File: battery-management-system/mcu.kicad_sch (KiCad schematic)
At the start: 34 parts, among them J11 I2C, J12 MCU_SUPPLY, J13 LEDS, J19 CHARGE/DISCHARGE, J20 UART_INTERCONNECT, J21 UART_USB, U14 STC3100, U4 STM32L071CZTx, U5 ARM-JTAG-SWD, U8 AT24C512C, U9 NCT75DR2G

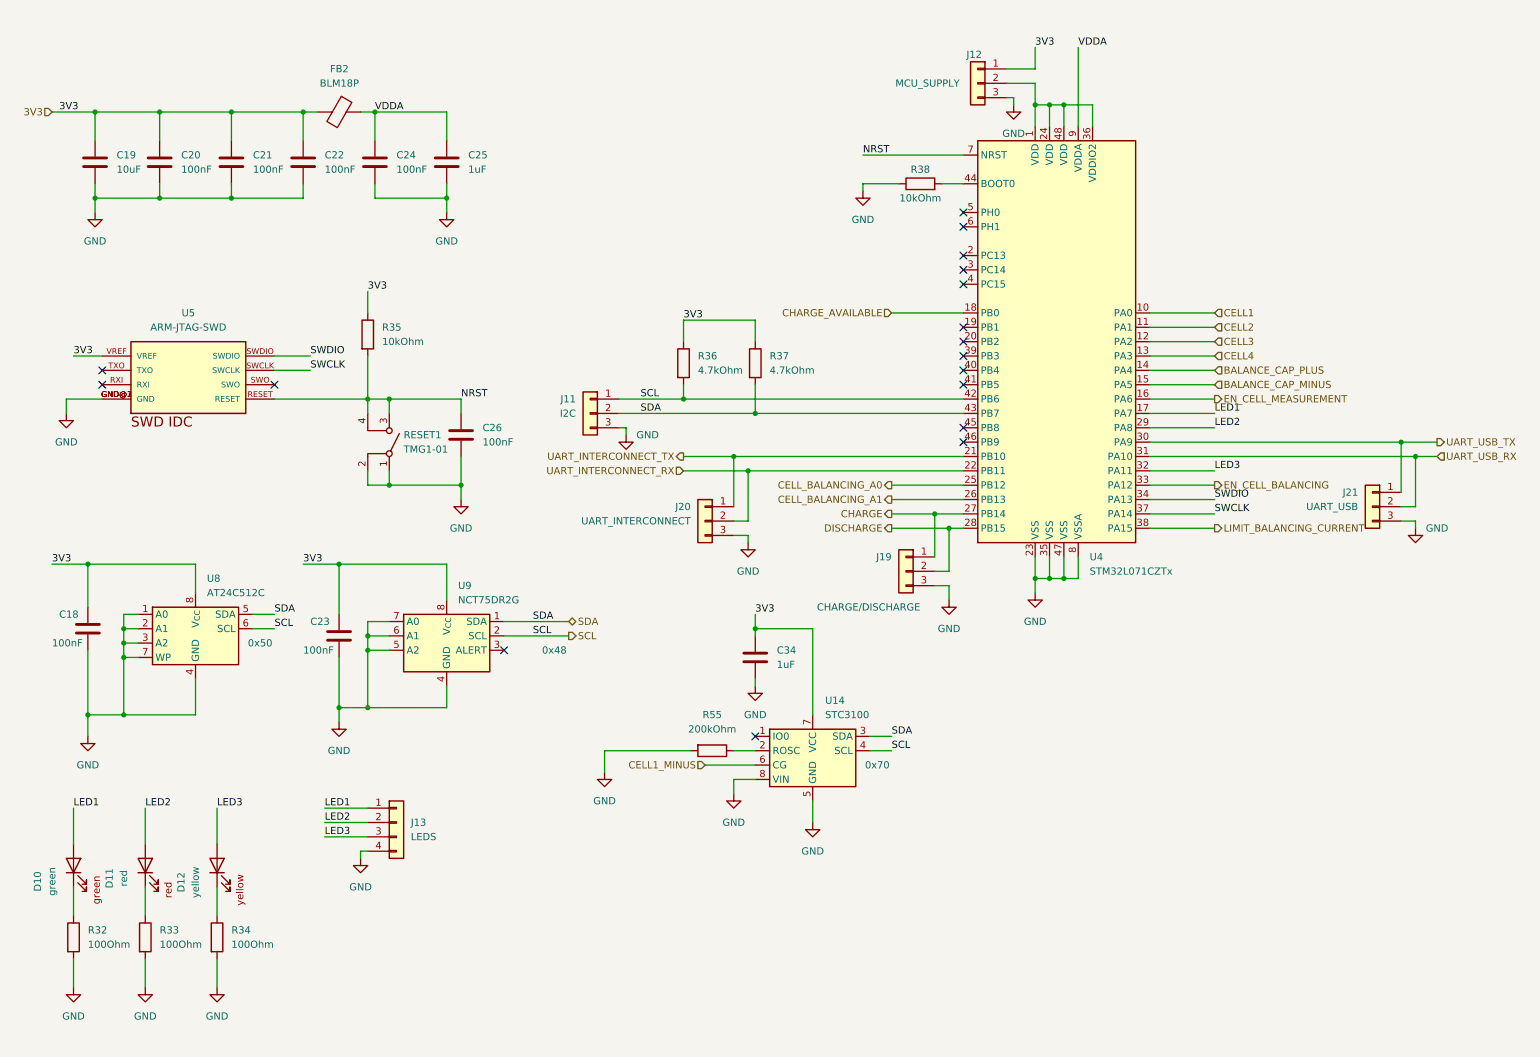
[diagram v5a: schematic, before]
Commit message: fix current sensing
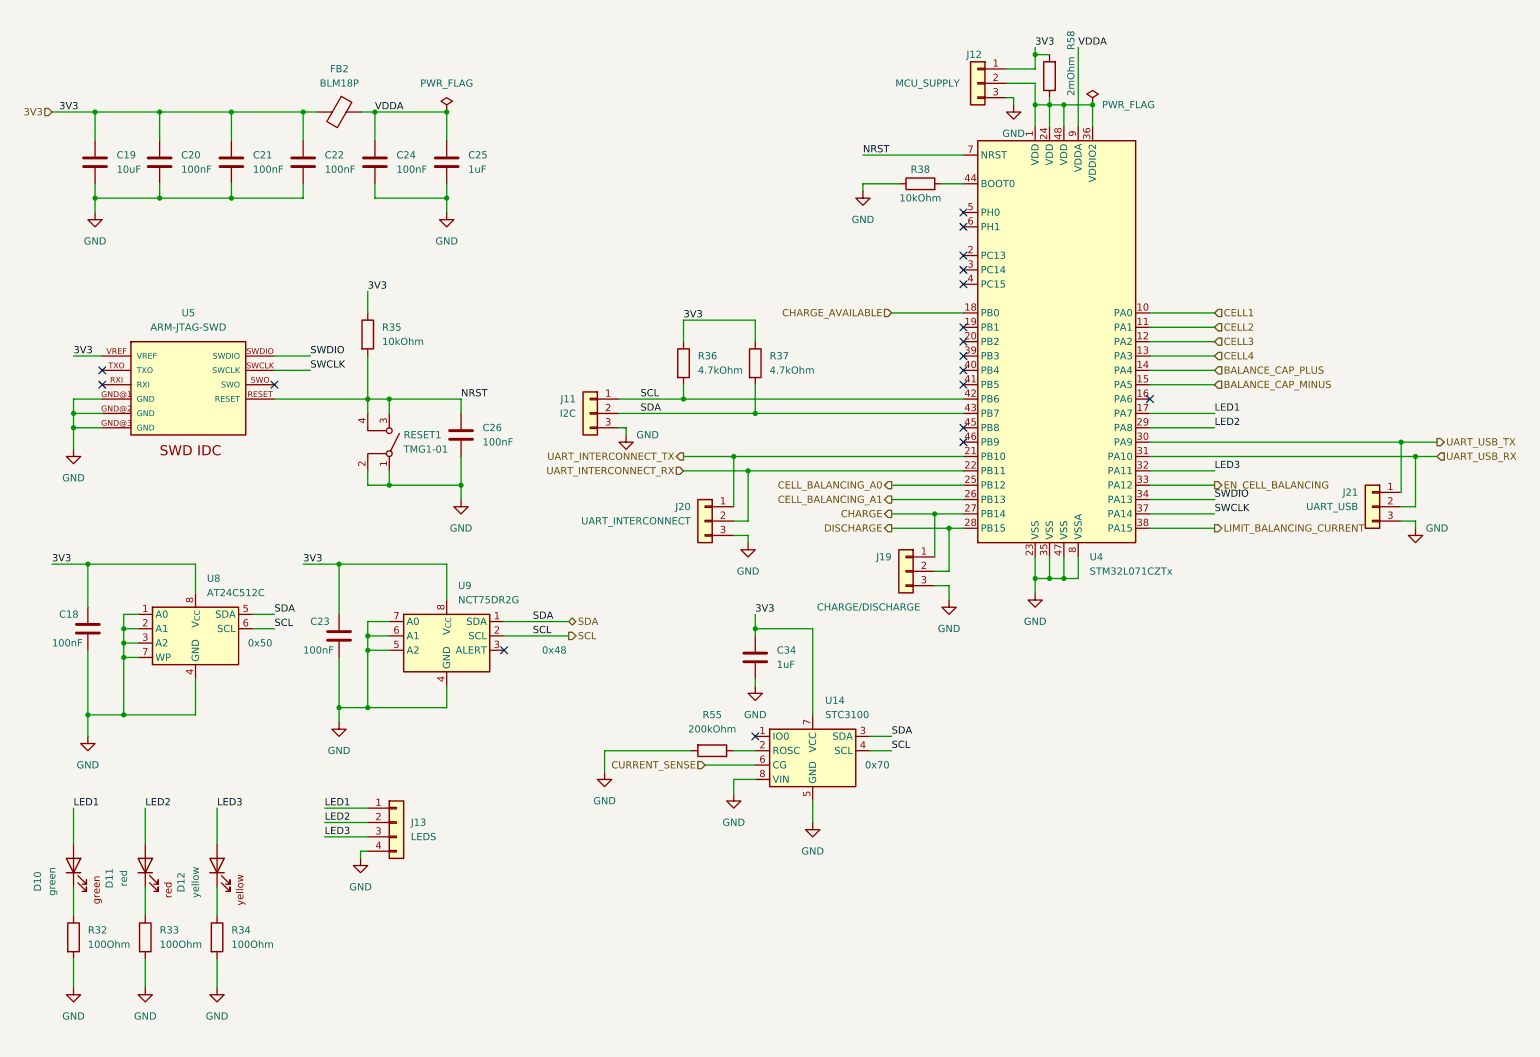
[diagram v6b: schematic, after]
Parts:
- added R58: 2mOhm, benediktibk:R_2512_6332Metric_Pad1.40x3.35mm_HandSolder, symbol benediktibk:R_2mOhm_SMD_2512_5W_1%
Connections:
- net 3V3: now also R58.2
- net at J12.2 (Pin_2), U4.1 (VDD), U4.24 (VDD)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: now also R58.1
- net CELL1_MINUS renamed CURRENT_SENSE
- net EN_CELL_MEASUREMENT: no longer names the net of U4.16 (PA6)
- no-connect marks 17 -> 18
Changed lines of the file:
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@@
   (junction (at 36.83 124.46) (diameter 0) (color 0 0 0 0)
   )
+  (junction (at 27.94 86.36) (diameter 0) (color 0 0 0 0)
+  )
   (junction (at 43.18 30.48) (diameter 0) (color 0 0 0 0)
   )
+  (junction (at 27.94 83.82) (diameter 0) (color 0 0 0 0)
+  )
   (junction (at 203.2 113.03) (diameter 0) (color 0 0 0 0)
   )
+  (junction (at 93.98 30.48) (diameter 0) (color 0 0 0 0)
+  )
   (junction (at 80.01 125.73) (diameter 0) (color 0 0 0 0)
   )
@@
   (junction (at 43.18 45.72) (diameter 0) (color 0 0 0 0)
   )
+  (junction (at 208.28 29.21) (diameter 0) (color 0 0 0 0)
+  )
   (junction (at 74.93 110.49) (diameter 0) (color 0 0 0 0)
   )
@@
   )
   (junction (at 198.12 29.21) (diameter 0) (color 0 0 0 0)
+  )
+  (junction (at 198.12 20.32) (diameter 0) (color 0 0 0 0)
   )
   (junction (at 68.58 30.48) (diameter 0) (color 0 0 0 0)
@@
   (no_connect (at 185.42 60.96))
   (no_connect (at 185.42 71.12))
+  (no_connect (at 218.44 81.28))
   (no_connect (at 185.42 55.88))
   (no_connect (at 185.42 78.74))
@@
     (stroke (width 0) (type default))
   )
+  (wire (pts (xy 200.66 27.94) (xy 200.66 29.21))
+    (stroke (width 0) (type default))
+  )
   (wire (pts (xy 125.73 86.36) (xy 124.46 86.36))
     (stroke (width 0) (type default))
@@
     (stroke (width 0) (type default))
   )
+  (wire (pts (xy 27.94 86.36) (xy 33.02 86.36))
+    (stroke (width 0) (type default))
+  )
   (wire (pts (xy 135.89 93.98) (xy 147.32 93.98))
     (stroke (width 0) (type default))
@@
     (stroke (width 0) (type default))
   )
-  (wire (pts (xy 218.44 81.28) (xy 229.87 81.28))
-    (stroke (width 0) (type default))
-  )
   (wire (pts (xy 55.88 45.72) (xy 68.58 45.72))
     (stroke (width 0) (type default))
@@
     (stroke (width 0) (type default))
   )
-  (wire (pts (xy 33.02 81.28) (xy 26.67 81.28))
+  (wire (pts (xy 33.02 81.28) (xy 27.94 81.28))
     (stroke (width 0) (type default))
   )
@@
     (stroke (width 0) (type default))
   )
-  (wire (pts (xy 26.67 81.28) (xy 26.67 83.82))
+  (wire (pts (xy 27.94 81.28) (xy 27.94 83.82))
     (stroke (width 0) (type default))
   )
@@
     (stroke (width 0) (type default))
   )
+  (wire (pts (xy 198.12 20.32) (xy 200.66 20.32))
+    (stroke (width 0) (type default))
+  )
   (wire (pts (xy 182.88 114.3) (xy 180.34 114.3))
     (stroke (width 0) (type default))
@@
     (stroke (width 0) (type default))
   )
+  (wire (pts (xy 27.94 83.82) (xy 33.02 83.82))
+    (stroke (width 0) (type default))
+  )
   (wire (pts (xy 36.83 137.16) (xy 49.53 137.16))
     (stroke (width 0) (type default))
@@
     (stroke (width 0) (type default))
   )
-  (wire (pts (xy 198.12 19.05) (xy 198.12 22.86))
+  (wire (pts (xy 198.12 19.05) (xy 198.12 20.32))
     (stroke (width 0) (type default))
   )
@@
     (stroke (width 0) (type default))
   )
+  (wire (pts (xy 27.94 83.82) (xy 27.94 86.36))
+    (stroke (width 0) (type default))
+  )
   (wire (pts (xy 36.83 127) (xy 36.83 124.46))
     (stroke (width 0) (type default))
@@
     (stroke (width 0) (type default))
   )
+  (wire (pts (xy 198.12 20.32) (xy 198.12 22.86))
+    (stroke (width 0) (type default))
+  )
   (wire (pts (xy 80.01 93.98) (xy 80.01 96.52))
     (stroke (width 0) (type default))
@@
   )
   (wire (pts (xy 30.48 137.16) (xy 36.83 137.16))
+    (stroke (width 0) (type default))
+  )
+  (wire (pts (xy 27.94 86.36) (xy 27.94 90.17))
     (stroke (width 0) (type default))
   )
@@
     (effects (font (size 1.27 1.27)) (justify left))
   )
-  (hierarchical_label "EN_CELL_MEASUREMENT" (shape output) (at 229.87 81.28 0) (fields_autoplaced)
-    (effects (font (size 1.27 1.27)) (justify left))
-  )
   (hierarchical_label "3V3" (shape input) (at 24.13 30.48 180) (fields_autoplaced)
     (effects (font (size 1.27 1.27)) (justify right))
@@
     (effects (font (size 1.27 1.27)) (justify left))
   )
-  (hierarchical_label "CELL1_MINUS" (shape input) (at 139.7 146.05 180) (fields_autoplaced)
+  (hierarchical_label "CURRENT_SENSE" (shape input) (at 139.7 146.05 180) (fields_autoplaced)
     (effects (font (size 1.27 1.27)) (justify right))
   )
@@
         (path "/5272f0ff-3069-41a9-bca2-80beede8b4b2/409f87d1-afa6-40d2-ba42-d5009501b8f9"
           (reference "C20") (unit 1)
+        )
+      )
+    )
+  )
+  (symbol (lib_id "power:PWR_FLAG") (at 93.98 30.48 0) (unit 1)
+    (in_bom yes) (on_board yes) (dnp no) (fields_autoplaced)
+    (property "Reference" "#FLG05" (at 93.98 28.575 0)
+      (effects (font (size 1.27 1.27)) hide)
+    )
+    (property "Value" "PWR_FLAG" (at 93.98 25.4 0)
+      (effects (font (size 1.27 1.27)))
+    )
+    (property "Footprint" "" (at 93.98 30.48 0)
+      (effects (font (size 1.27 1.27)) hide)
+    )
+    (property "Datasheet" "~" (at 93.98 30.48 0)
+      (effects (font (size 1.27 1.27)) hide)
+    )
+    (pin "1")
+    (instances
+      (project "battery-management-system"
+        (path "/5272f0ff-3069-41a9-bca2-80beede8b4b2/afdb149d-bd78-484c-a496-c5b66260efca"
+          (reference "#FLG05") (unit 1)
+        )
+        (path "/5272f0ff-3069-41a9-bca2-80beede8b4b2/409f87d1-afa6-40d2-ba42-d5009501b8f9"
+          (reference "#FLG06") (unit 1)
         )
       )
@@
     )
   )
+  (symbol (lib_id "power:PWR_FLAG") (at 208.28 29.21 0) (unit 1)
+    (in_bom yes) (on_board yes) (dnp no)
+    (property "Reference" "#FLG05" (at 208.28 27.305 0)
+      (effects (font (size 1.27 1.27)) hide)
+    )
+    (property "Value" "PWR_FLAG" (at 214.63 29.21 0)
+      (effects (font (size 1.27 1.27)))
+    )
+    (property "Footprint" "" (at 208.28 29.21 0)
+      (effects (font (size 1.27 1.27)) hide)
+    )
+    (property "Datasheet" "~" (at 208.28 29.21 0)
+      (effects (font (size 1.27 1.27)) hide)
+    )
+    (pin "1")
+    (instances
+      (project "battery-management-system"
+        (path "/5272f0ff-3069-41a9-bca2-80beede8b4b2/afdb149d-bd78-484c-a496-c5b66260efca"
+          (reference "#FLG05") (unit 1)
+        )
+        (path "/5272f0ff-3069-41a9-bca2-80beede8b4b2/409f87d1-afa6-40d2-ba42-d5009501b8f9"
+          (reference "#FLG07") (unit 1)
+        )
+      )
+    )
+  )
   (symbol (lib_id "power:GND") (at 93.98 48.26 0) (unit 1)
     (in_bom yes) (on_board yes) (dnp no) (fields_autoplaced)
@@
     )
   )
-  (symbol (lib_id "power:GND") (at 26.67 83.82 0) (unit 1)
-    (in_bom yes) (on_board yes) (dnp no) (fields_autoplaced)
-    (property "Reference" "#PWR0138" (at 26.67 90.17 0)
-      (effects (font (size 1.27 1.27)) hide)
-    )
-    (property "Value" "GND" (at 26.67 88.9 0)
-      (effects (font (size 1.27 1.27)))
-    )
-    (property "Footprint" "" (at 26.67 83.82 0)
-      (effects (font (size 1.27 1.27)) hide)
-    )
-    (property "Datasheet" "" (at 26.67 83.82 0)
+  (symbol (lib_id "power:GND") (at 27.94 90.17 0) (unit 1)
+    (in_bom yes) (on_board yes) (dnp no) (fields_autoplaced)
+    (property "Reference" "#PWR0138" (at 27.94 96.52 0)
+      (effects (font (size 1.27 1.27)) hide)
+    )
+    (property "Value" "GND" (at 27.94 95.25 0)
+      (effects (font (size 1.27 1.27)))
+    )
+    (property "Footprint" "" (at 27.94 90.17 0)
+      (effects (font (size 1.27 1.27)) hide)
+    )
+    (property "Datasheet" "" (at 27.94 90.17 0)
       (effects (font (size 1.27 1.27)) hide)
     )
@@
         )
       )
+    )
+  )
+  (symbol (lib_id "benediktibk:R_2mOhm_SMD_2512_5W_1%") (at 200.66 24.13 180) (unit 1)
+    (in_bom yes) (on_board yes) (dnp no)
+    (property "Reference" "R58" (at 204.47 17.78 90)
+      (effects (font (size 1.27 1.27)))
+    )
+    (property "Value" "2mOhm" (at 204.47 24.13 90)
+      (effects (font (size 1.27 1.27)))
+    )
+    (property "Footprint" "benediktibk:R_2512_6332Metric_Pad1.40x3.35mm_HandSolder" (at 210.82 24.638 90)
+      (effects (font (size 1.27 1.27)) hide)
+    )
+    (property "Datasheet" "~" (at 200.66 24.13 0)
+      (effects (font (size 1.27 1.27)) hide)
+    )
+    (property "RS order number" "231-3683" (at 218.44 25.4 0)
+      (effects (font (size 1.27 1.27)) hide)
+    )
+    (pin "1")
+    (pin "2")
+    (instances
+      (project "battery-management-system"
+        (path "/5272f0ff-3069-41a9-bca2-80beede8b4b2/b1377397-46a1-4623-af59-88e4e694ca35"
+          (reference "R58") (unit 1)
+        )
+        (path "/5272f0ff-3069-41a9-bca2-80beede8b4b2/409f87d1-afa6-40d2-ba42-d5009501b8f9"
+          (reference "R59") (unit 1)
+        )
+      )

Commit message: apply recommendations of Stefan
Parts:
- removed R33: 100Ohm, benediktibk:R_0603_1608Metric_Pad0.98x0.95mm_HandSolder, symbol benediktibk:R_100Ohm_SMD_0603_100mW_1%
- added C48: 100nF, benediktibk:C_0603_1608Metric_Pad1.08x0.95mm_HandSolder, symbol benediktibk:C_100nF_SMD_0603_50V
- added Q5 (x3): DMN3730U, benediktibk:SOT-23, symbol benediktibk:DMN3730U
- added R33, R53, R58: 10kOhm, benediktibk:R_0603_1608Metric_Pad0.98x0.95mm_HandSolder, symbol benediktibk:R_10kOhm_SMD_0603_100mW_1%
- added R60: 100Ohm, benediktibk:R_0603_1608Metric_Pad0.98x0.95mm_HandSolder, symbol benediktibk:R_100Ohm_SMD_0603_100mW_1%
- added R61, R62, R63, R64: 0Ohm, benediktibk:R_0603_1608Metric_Pad0.98x0.95mm_HandSolder, symbol benediktibk:R_0Ohm_SMD_0603_100mW_0%
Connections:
- net 3V3: now also D10.2 (A), D11.2 (A), D12.2 (A), J12.2 (Pin_2), R58.1, U4.1 (VDD), U4.24 (VDD), U4.36 (VDDIO2), U4.48 (VDD), C48.1
- net GND: now also C48.2, Q5.2 (S), Q5.2 (S), Q5.2 (S), R33.1, R53.1, R58.1; no longer R32.2, R34.2
- net LED1: now also Q5.1 (G), R53.2; no longer D10.2 (A)
- net LED2: now also Q5.1 (G), R33.2; no longer D11.2 (A)
- net LED3: now also Q5.1 (G), R58.2; no longer D12.2 (A)
- net UART_INTERCONNECT_RX: now also R62.1; no longer U4.22 (PB11)
- net UART_INTERCONNECT_TX: now also R61.1; no longer U4.21 (PB10)
- net UART_USB_RX: now also R63.2; no longer U4.31 (PA10)
- net UART_USB_TX: now also R64.2; no longer U4.30 (PA9)
- net at D12.1 (K): now also R60.1; no longer R34.1
- net at D11.1 (K): now also R34.1
- new net: Q5.3 (D), R32.2
- new net: R61.2, U4.21 (PB10)
- new net: Q5.3 (D), R60.2
- new net: R63.1, U4.31 (PA10)
- new net: Q5.3 (D), R34.2
- new net: R64.1, U4.30 (PA9)
- new net: R62.2, U4.22 (PB11)
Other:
- moved on the sheet: C19, C20, C21, C22, C24, C25, D10, D11, D12, FB2, J12, J13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

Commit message: improve layout
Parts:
- renumbered C18 to C22, C19 to C23, C20 to C24, C23 to C25, C21 to C26, C48 to C27, C26 to C28, C22 to C29, C24 to C30, C25 to C31, C34 to C32, D10 to D19, D11 to D20, D12 to D21, J12 to J15, J11 to J16, J20 to J17, J13 to J18, J21 to J20, R53 to R27, R32 to R29, R33 to R30, R34 to R31, R35 to R32, R58 to R33, R60 to R34, R36 to R35, R55 to R36, R62 to R38, R61 to R39, R38 to R40, R63 to R41, R64 to R42, U14 to U10, U4 to U11, U5 to U7
